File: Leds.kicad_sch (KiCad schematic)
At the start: 25 parts

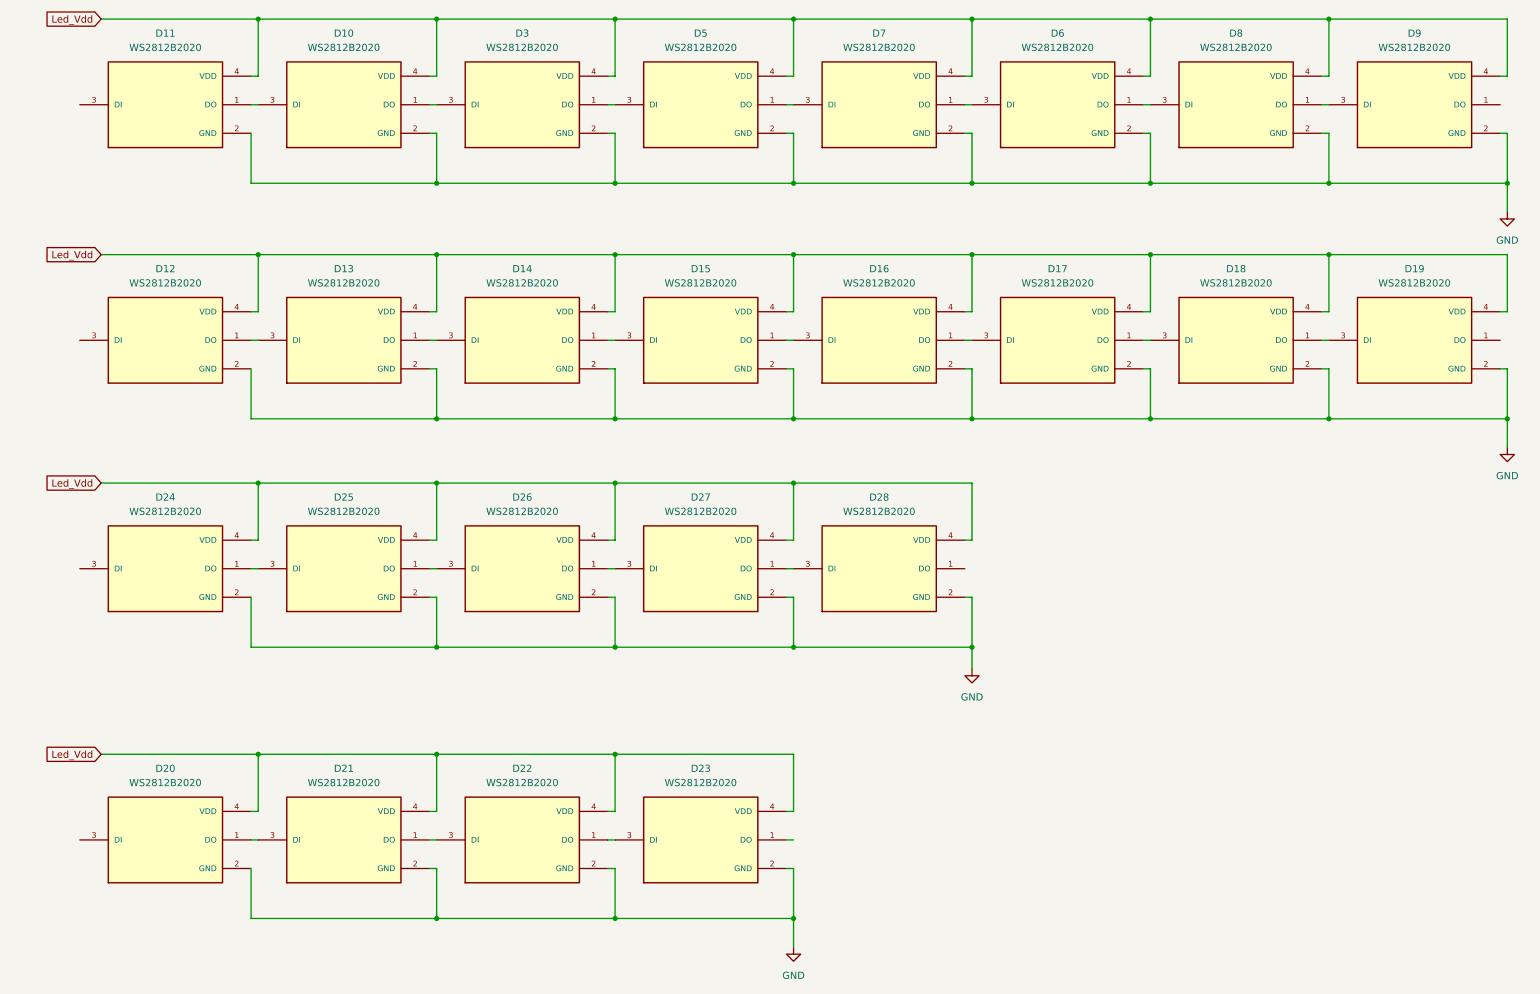
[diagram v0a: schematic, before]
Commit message: feat(PCB): start of castellated edges implementation
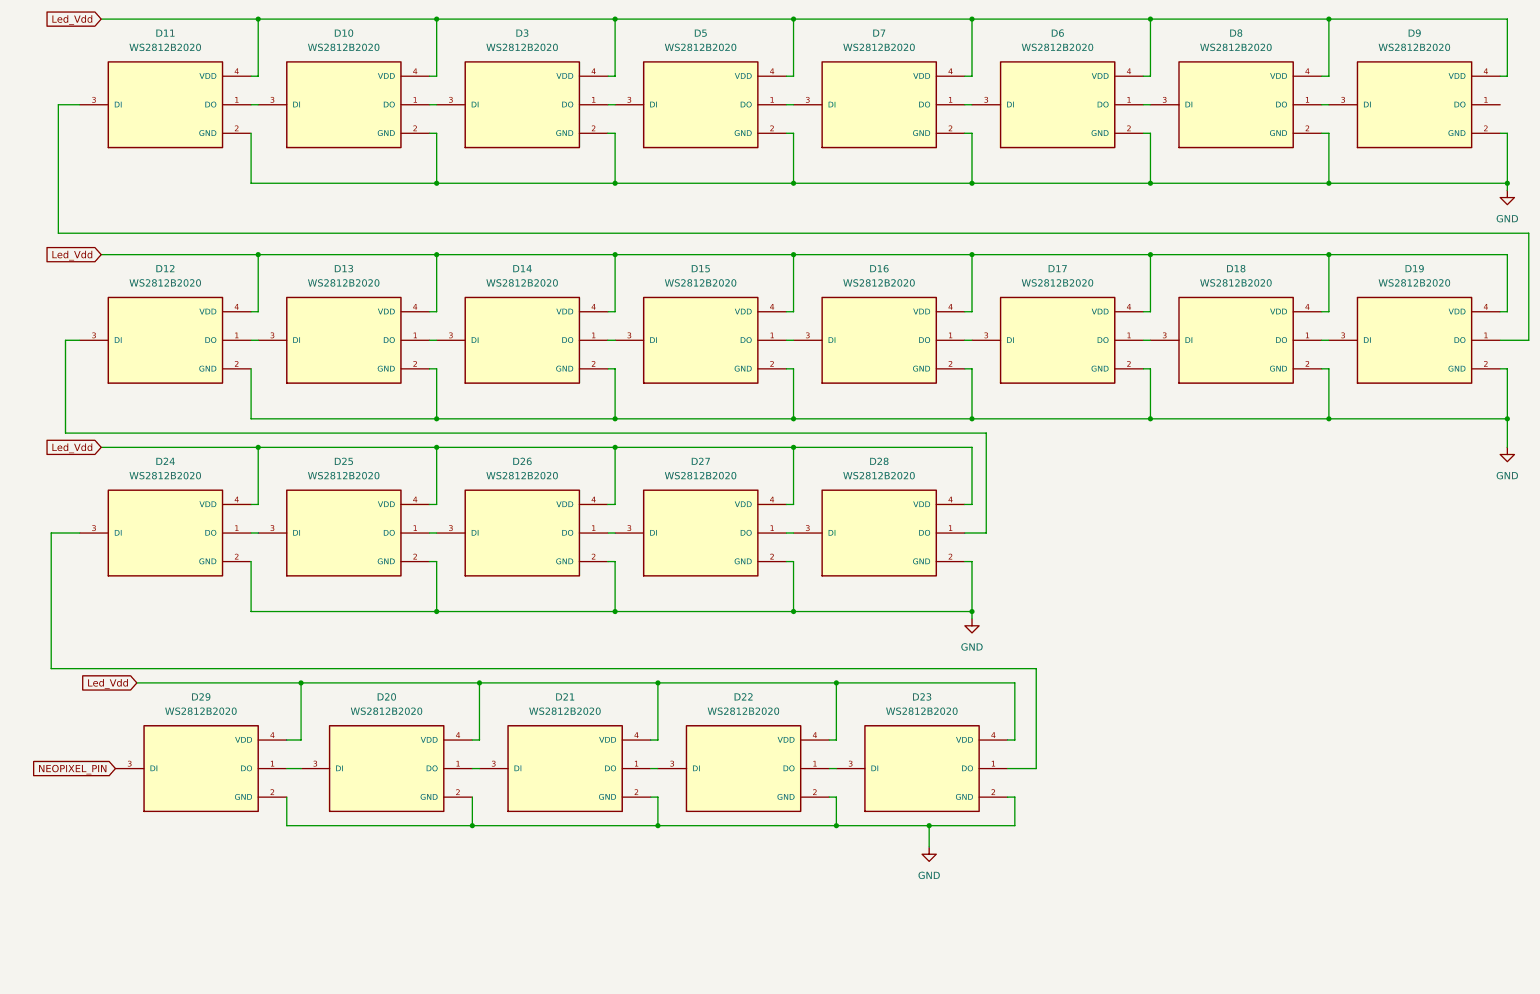
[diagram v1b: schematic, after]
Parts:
- added D29: WS2812B2020, WS2812B2020:LED_WS2812B2020, symbol WS2812B2020:WS2812B2020
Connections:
- net GND: now also D29.2 (GND)
- net Led_Vdd: now also D29.4 (VDD)
- net at D24.3 (DI): now also D23.1 (DO)
- net at D19.1 (DO): now also D11.3 (DI)
- net at D12.3 (DI): now also D28.1 (DO)
- net at D20.3 (DI): now also D29.1 (DO)
- new net NEOPIXEL_PIN: D29.3 (DI)
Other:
- moved on the sheet: D20, D21, D22, D23, D24, D25, D26, D27, D28

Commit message: feat(PCB): finalized initial PCB
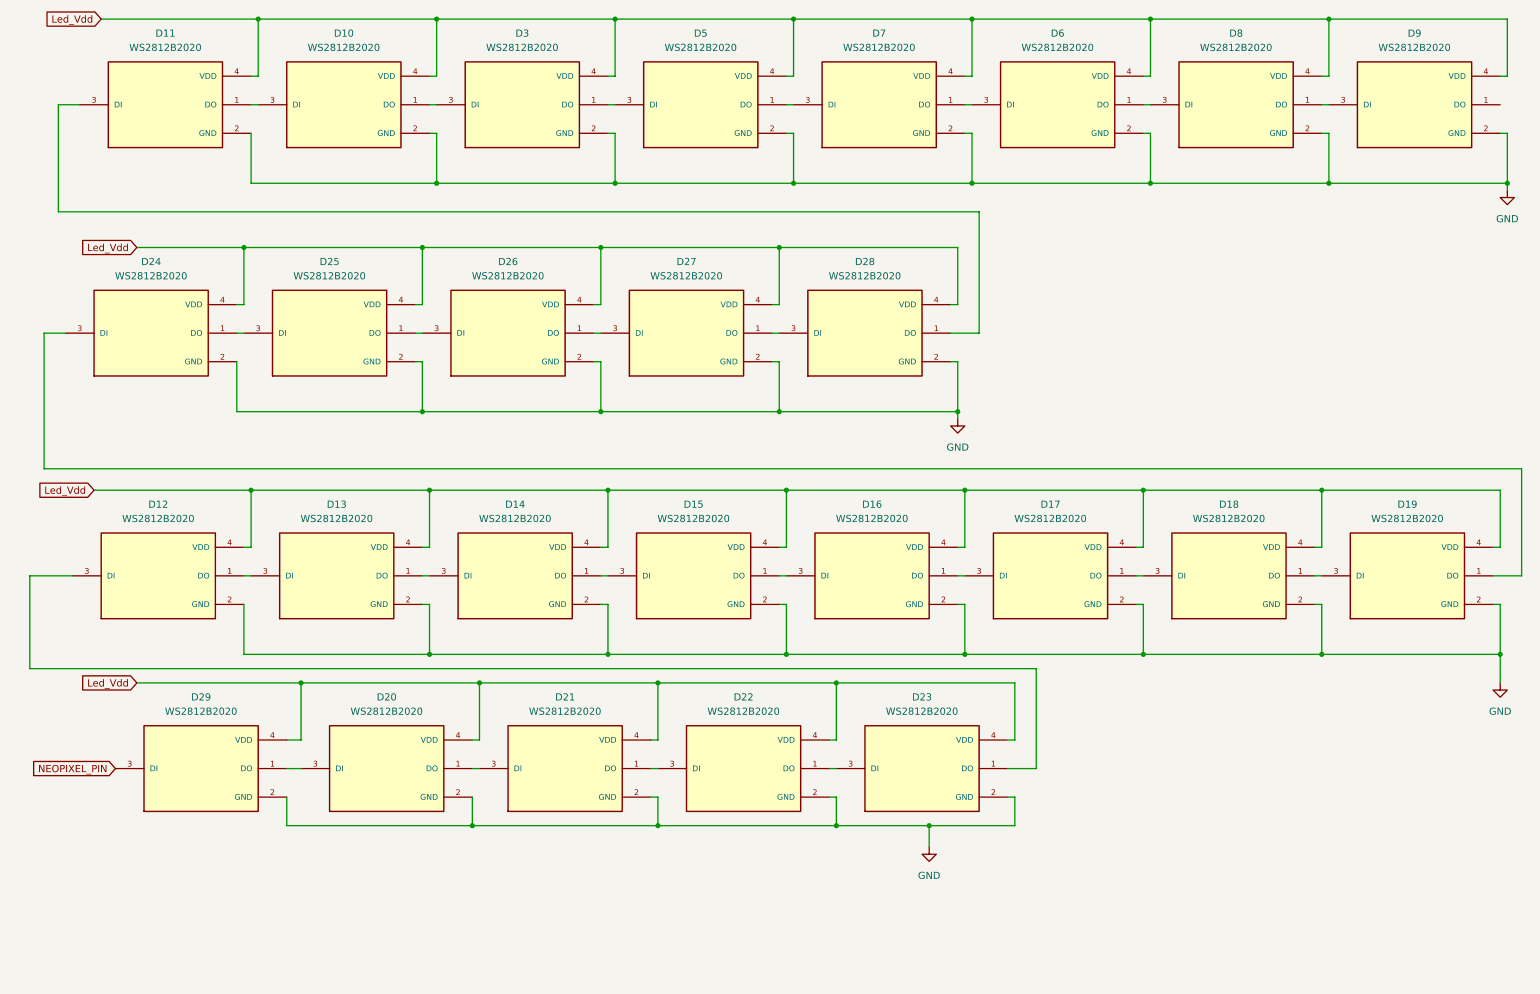
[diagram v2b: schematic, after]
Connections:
- net at D24.3 (DI): now also D19.1 (DO); no longer D23.1 (DO)
- net at D11.3 (DI): now also D28.1 (DO); no longer D19.1 (DO)
- net at D12.3 (DI): now also D23.1 (DO); no longer D28.1 (DO)
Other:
- moved on the sheet: D12, D13, D14, D15, D16, D17, D18, D19, D24, D25, D26, D27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

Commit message: chore(PCB): Final Version
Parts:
- added C10, C5, C6, C9: 0.4u, Capacitor_SMD:C_0201_0603Metric, symbol Device:C
- added C11, C12, C7, C8: 0.2u, Capacitor_SMD:C_0201_0603Metric, symbol Device:C
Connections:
- net GND: now also C10.2, C11.2, C12.2, C5.2, C6.2, C7.2, C8.2, C9.2
- net Led_Vdd: now also C10.1, C11.1, C12.1, C5.1, C6.1, C7.1, C8.1, C9.1
